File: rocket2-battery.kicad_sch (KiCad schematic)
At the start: 59 parts, among them J7 Conn_01x07, J8 SMA, J9 ARM Cortex Debug, P10 PAD_SMD, P5 PAD_SMD, P6 PAD_SMD, P7 PAD_SMD, P8 PAD_SMD, P9 PAD_SMD, Q2 Q_NMOS_GSD, Q3 Q_NMOS_GSD, Q4 PMOS, Q5 PMOS, Q6 Q_NMOS_GSD, Q7 Q_NMOS_GSD, Q8 PMOS, Q9 PMOS, U10 3V3 LDO, Y1 16MHz

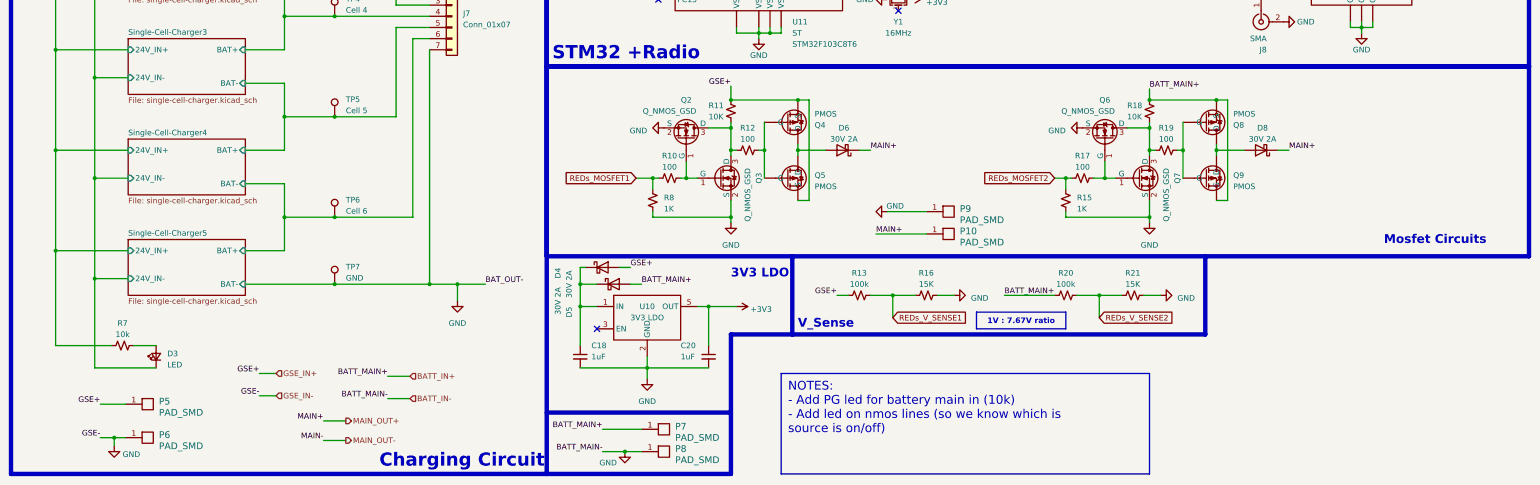
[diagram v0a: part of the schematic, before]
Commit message: Updated so only STM pins left really
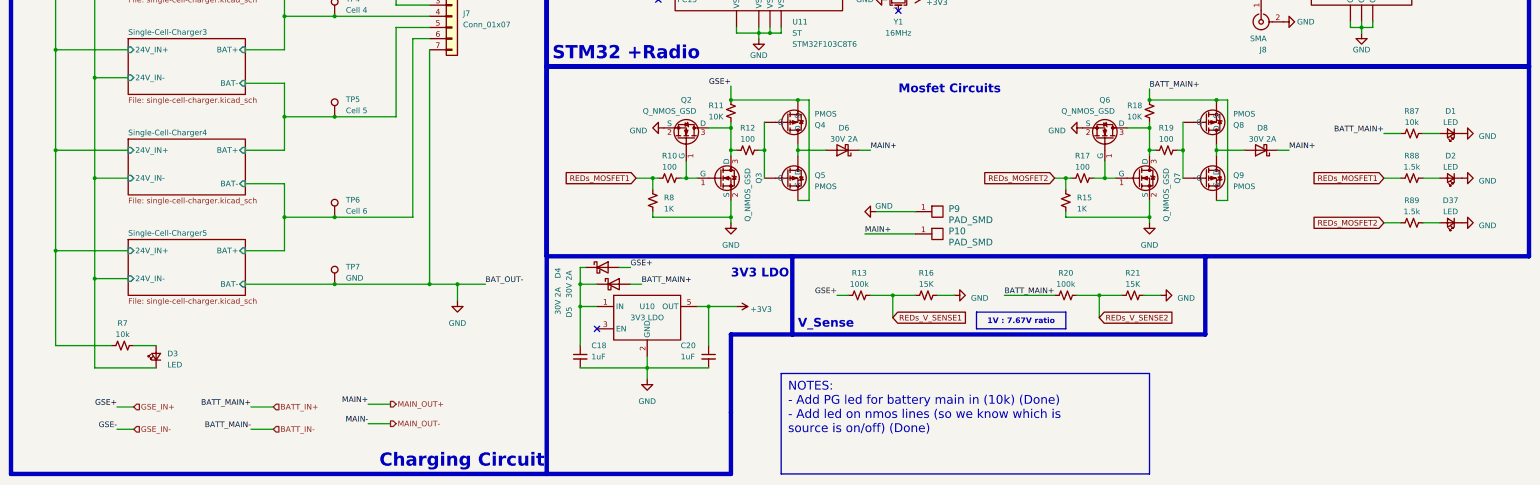
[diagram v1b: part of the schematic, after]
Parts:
- removed P5, P6, P7, P8: PAD_SMD, TestPoint:TestPoint_Pad_2.0x2.0mm, symbol pkl_misc:PAD_SMD
- added D1, D2, D37: LED, LED_SMD:LED_0603_1608Metric_Pad1.05x0.95mm_HandSolder, symbol Device:LED_Small
- added R87: 10k, Resistor_SMD:R_0603_1608Metric_Pad0.98x0.95mm_HandSolder, symbol Device:R_Small_US
- added R88, R89: 1.5k, Resistor_SMD:R_0603_1608Metric_Pad0.98x0.95mm_HandSolder, symbol Device:R_Small_US
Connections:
- net BATT_IN+: now also R87.1
- net GND: now also D1.1 (K), D2.1 (K), D37.1 (K); no longer D3.1 (K)
- net REDs_MOSFET1: now also R88.1
- net REDs_MOSFET2: now also R89.1
- new net: D2.2 (A), R88.2
- new net: D1.2 (A), R87.2
- new net: D37.2 (A), R89.2
- new net GSE_IN-: D3.1 (K)
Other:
- moved on the sheet: P10, P9

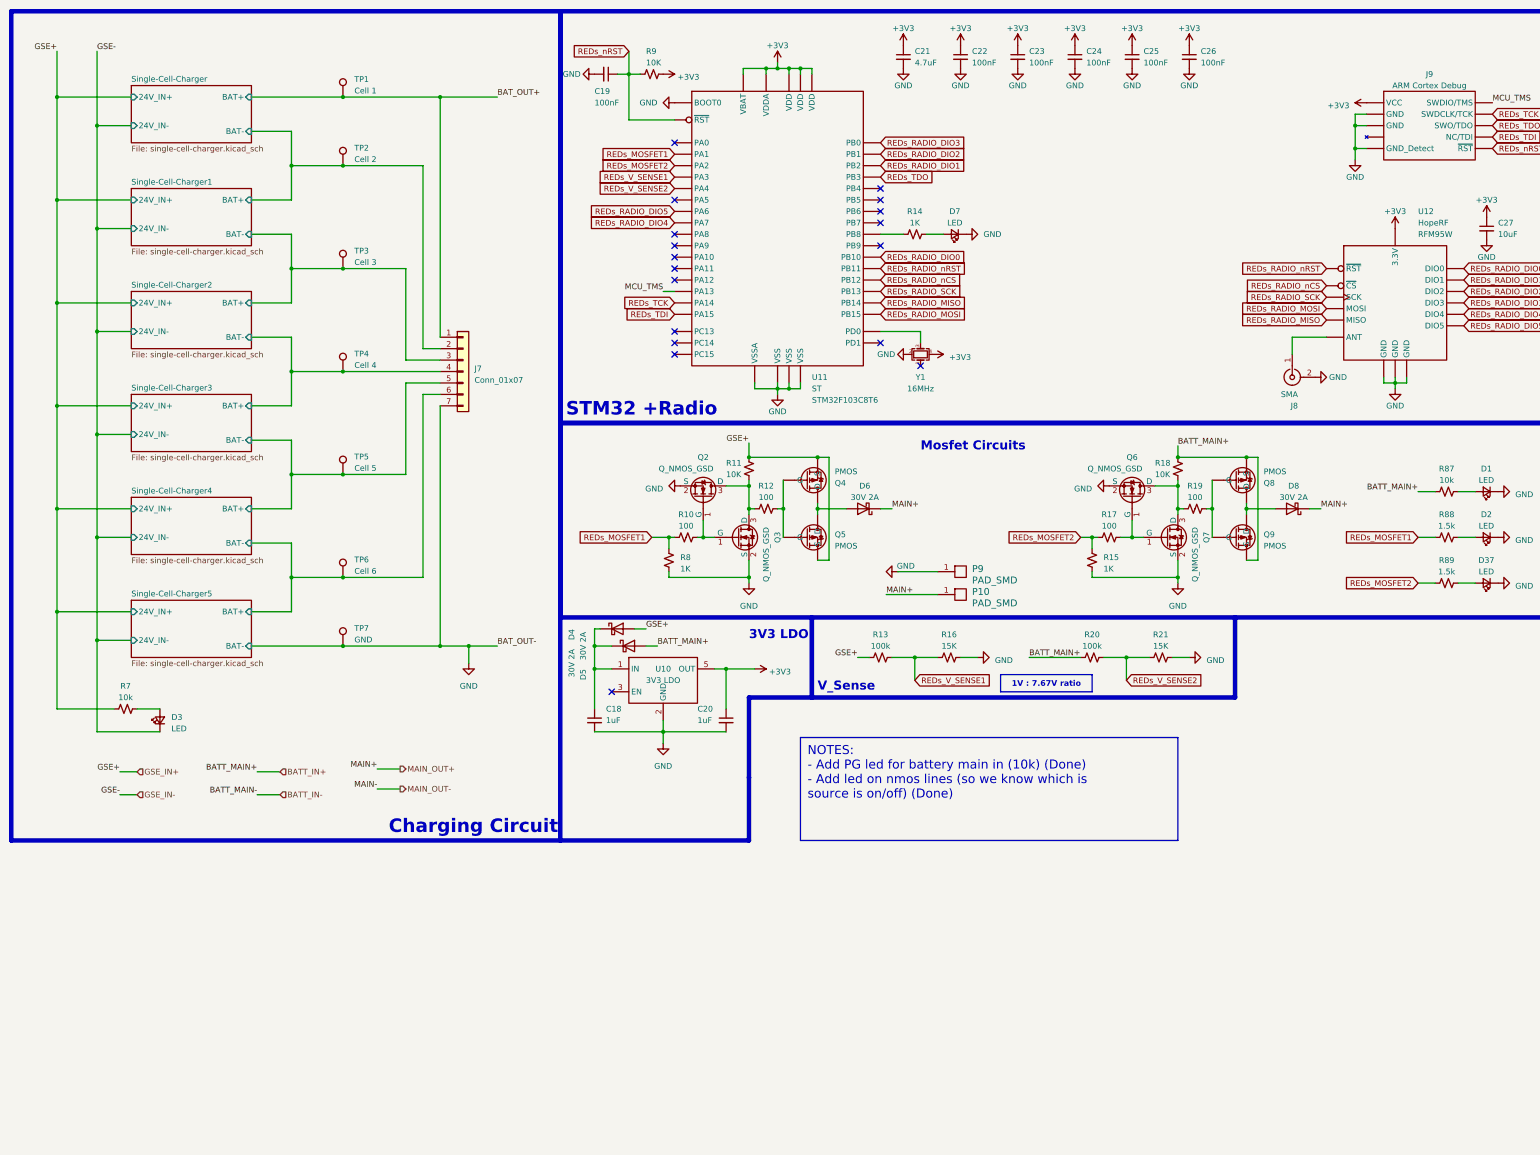
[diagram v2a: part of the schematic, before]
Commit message: Added stat sense in REDs; kicad V8.01
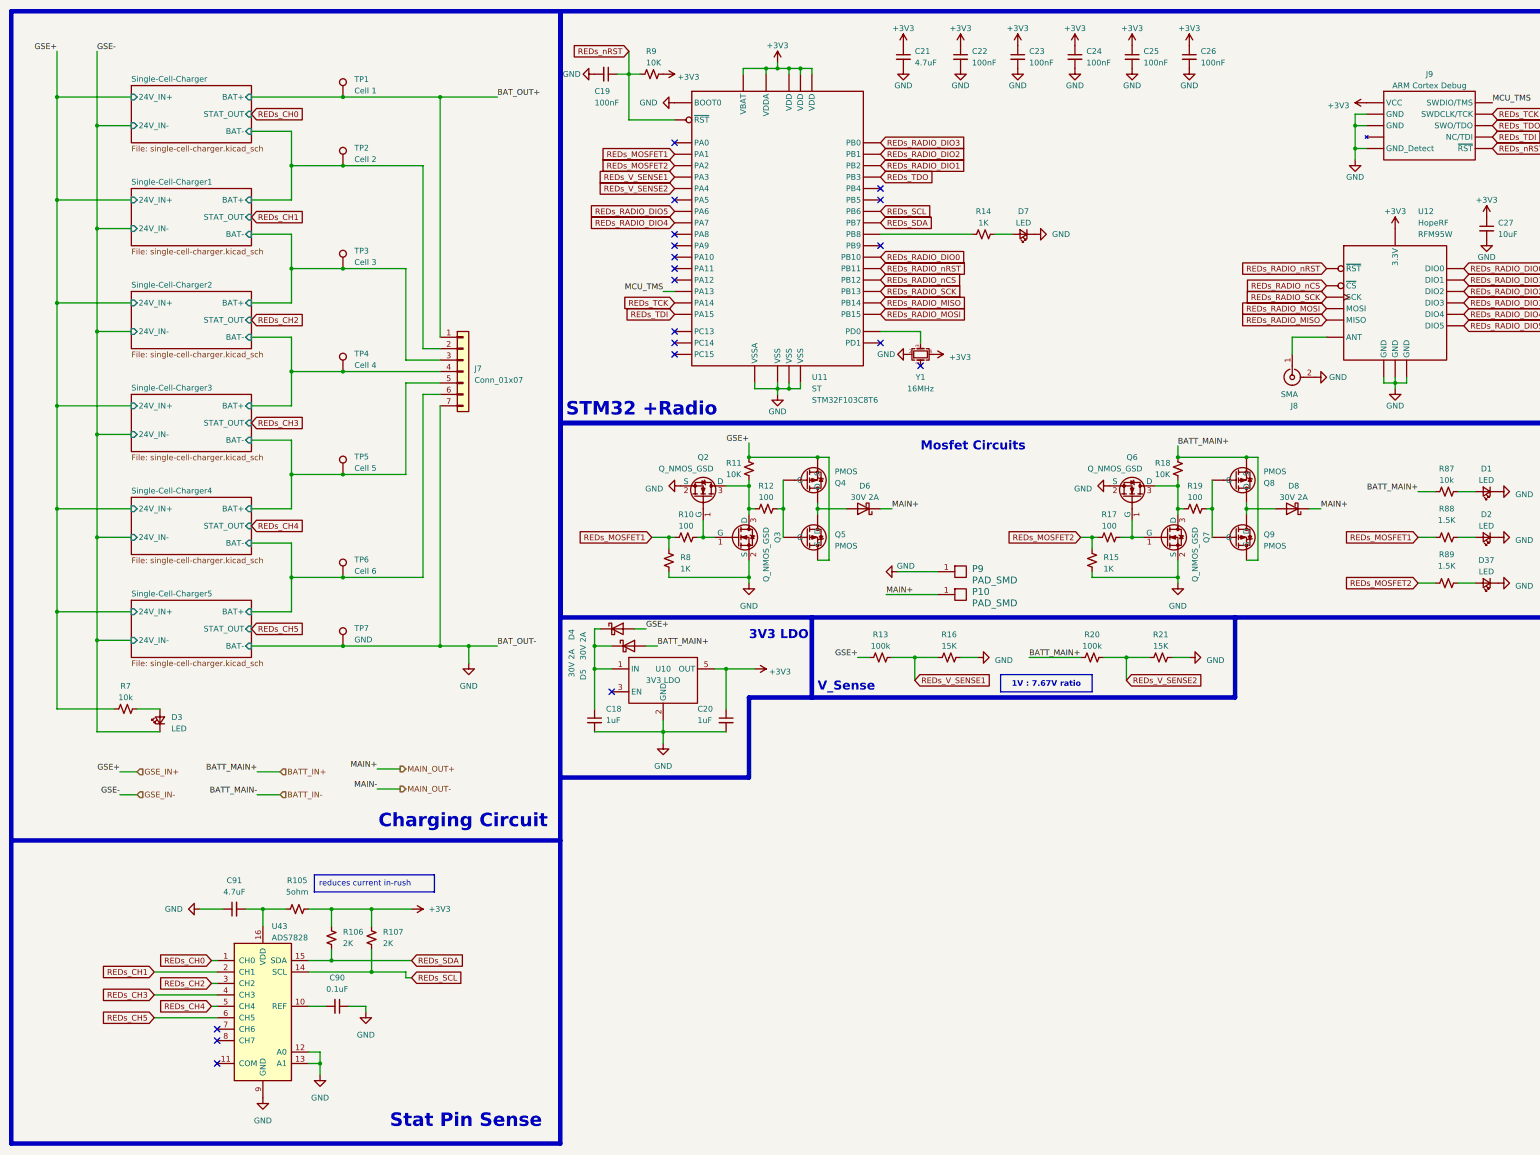
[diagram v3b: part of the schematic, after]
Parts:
- added C90: 0.1uF, symbol Device:C_Small
- added C91: 4.7uF, symbol Device:C_Small
- added R105: 5ohm, symbol Device:R_Small_US
- added R106, R107: 2K, symbol Device:R_Small_US
- added U43: ADS7828, Package_SO:TSSOP-16_4.4x5mm_P0.65mm, symbol Analog_ADC:ADS7828
- R88, R89: value 1.5k -> 1.5K
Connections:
- net +3V3: now also R105.2, R106.1, R107.1
- net GND: now also C90.1, C91.1, U43.12 (A0), U43.13 (A1), U43.9 (GND)
- net REDs_SCL: now reaches U11.42 (PB6)
- net REDs_SCL: now also R107.2, U43.14 (SCL)
- net REDs_SDA: now reaches U11.43 (PB7)
- net REDs_SDA: now also R106.2, U43.15 (SDA)
- new net: C90.2, U43.10 (REF)
- new net: C91.2, R105.1, U43.16 (VDD)
- new net REDs_CH0: U43.1 (CH0)
- new net REDs_CH1: U43.2 (CH1)
- new net REDs_CH2: U43.3 (CH2)
- new net REDs_CH3: U43.4 (CH3)
- new net REDs_CH4: U43.5 (CH4)
- new net REDs_CH5: U43.6 (CH5)
- no-connect marks 18 -> 19
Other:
- sheet Single-Cell-Charger ports: added STAT_OUT; removed none
- sheet Single-Cell-Charger1 ports: added STAT_OUT; removed none
- sheet Single-Cell-Charger2 ports: added STAT_OUT; removed none
- sheet Single-Cell-Charger3 ports: added STAT_OUT; removed none
- sheet Single-Cell-Charger4 ports: added STAT_OUT; removed none
- sheet Single-Cell-Charger5 ports: added STAT_OUT; removed none
- note added: "Stat Pin Sense"
- moved on the sheet: D7, R14

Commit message: 8.02 Update; Also changed VRMs and added some notes
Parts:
- renumbered C90 to C10, C18 to C11, C19 to C12, C20 to C13, C21 to C14, C22 to C15, C23 to C16, C24 to C17, C25 to C18, C26 to C19, C27 to C20, C91 to C9, D3 to D1, D4 to D2, D5 to D3, D6 to D4, D7 to D5, D8 to D6, D1 to D7, D2 to D8, D37 to D9, J7 to J3, J8 to J4, J9 to J5, P9 to P5, P10 to P6, R8 to R10, R10 to R11, R11 to R12, R12 to R13, R13 to R14, R16 to R15, R14 to R16, R15 to R17, R20 to R18, R17 to R19, R21 to R20, R18 to R21, R19 to R22, R87 to R23, R88 to R24, R89 to R25, R7 to R5, R105 to R6, R106 to R7, R107 to R8, U12 to U10, U43 to U7, U10 to U8, U11 to U9
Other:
- note added: "ONCE ROCKET IS LAUNCHED, IN NO CASE SHOULD IT KILL POWER. HOW TO ENSURE????"

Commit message: ECU essentially reviewable
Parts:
- removed C11, C13: 1uF, Capacitor_SMD:C_0603_1608Metric_Pad1.08x0.95mm_HandSolder, symbol Device:C_Small
- removed U8: 3V3 LDO, Package_SO:TSOP-5_1.65x3.05mm_P0.95mm, symbol UCIRP-KiCAD-Lib:NCV8730
- added C10, C11: 100uF, symbol Device:C_Polarized_Small
- added C12: 680uF, symbol Device:C_Polarized_Small
- added C13: 330uF, symbol Device:C_Polarized_Small
- added D10, D13, D9: LED, LED_SMD:LED_0603_1608Metric_Pad1.05x0.95mm_HandSolder, symbol Device:LED_Small
- added D4: 30V 2A, Diode_SMD:Nexperia_DSN1608-2_1.6x0.8mm, symbol Device:D_Schottky
- added D5: 30V 5A, Diode_SMD:D_SOD-128, symbol Device:D_Schottky
- added D6, D7: 700mV 5A, symbol Device:D_Schottky_Small
- added J3: USB_A, symbol Connector:USB_A
- added L1: 33uH, symbol Device:L_Small
- added L2: 68uH, symbol Device:L_Small
- added R17, R19: 1.5K, Resistor_SMD:R_0603_1608Metric_Pad0.98x0.95mm_HandSolder, symbol Device:R_Small_US
- added R25: 100k, Resistor_SMD:R_0603_1608Metric_Pad0.98x0.95mm_HandSolder, symbol Device:R_Small_US
- added R26: 10k, Resistor_SMD:R_0603_1608Metric_Pad0.98x0.95mm_HandSolder, symbol Device:R_Small_US
- added U6: LM2596S-3.3, Package_TO_SOT_SMD:TO-263-5_TabPin3, symbol Regulator_Switching:LM2596S-3.3
- added U7: LM2596S-5, Package_TO_SOT_SMD:TO-263-5_TabPin3, symbol Regulator_Switching:LM2596S-5
- D3: value 30V 2A -> 30V 5A; footprint Diode_SMD:Nexperia_DSN1608-2_1.6x0.8mm -> Diode_SMD:D_SOD-128; Manufacturer Onsemi -> Nexperia; Part # NSR20F30NXT5G -> PMEG3050EP,115
- U9: renamed from U10; Part # RFM95W -> RFM96W
- renumbered C9 to C7, C10 to C8, C12 to C9, D5 to D11, D6 to D12, D7 to D14, D8 to D15, D9 to D16, D4 to D8, J3 to J2, R9 to R10, R10 to R11, R11 to R12, R15 to R13, R12 to R14, R13 to R15, R18 to R16, R20 to R18, R16 to R20, R17 to R21, R19 to R22, R21 to R23, R22 to R24, R23 to R27, R24 to R28, R25 to R29, R14 to R9, U7 to U5, U9 to U8
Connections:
- net +3V3: now also C12.1, L1.2, R19.1, U6.4 (FB)
- net BATT_IN+: now also D4.2 (A), D5.2 (A); no longer D3.2 (A)
- net GND: now also C10.2, C11.2, C12.2, C13.2, D10.1 (K), D13.1 (K), D6.2 (A), D7.2 (A), D9.1 (K), J3.4 (GND), J3.5 (Shield), U6.3 (GND), U6.5 (~{ON}/OFF), U7.3 (GND), U7.5 (~{ON}/OFF)
- net GSE_IN+: now also D3.2 (A), R26.1
- net REDs_RADIO_DIO2: no longer U9.16 (DIO2)
- net REDs_RADIO_nCS: now also R25.2
- net at D3.1 (K): now also C11.1, D5.1 (K), U7.1 (VIN); no longer D2.1 (K)
- net REDs_RADIO_DIO3: no longer names the net of U9.11 (DIO3)
- net REDs_RADIO_DIO3: no longer U8.18 (PB0)
- net REDs_RADIO_DIO4: no longer names the net of U9.12 (DIO4)
- net REDs_RADIO_DIO4: no longer U8.17 (PA7)
- net REDs_RADIO_DIO5: no longer names the net of U9.7 (DIO5)
- net REDs_RADIO_DIO5: no longer U8.16 (PA6)
- new net: C13.1, J3.1 (VBUS), L2.2, R17.1, U7.4 (FB)
- new net: D9.2 (A), R17.2
- new net: D7.1 (K), L2.1, U7.2 (OUT)
- new net: D10.2 (A), R19.2
- new net: D6.1 (K), L1.1, U6.2 (OUT)
- new net: C10.1, D2.1 (K), D4.1 (K), U6.1 (VIN)
- new net: D13.2 (A), R26.2
- new net +3.3V: R25.1
- no-connect marks 19 -> 27
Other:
- note added: "3V3 REG"
- note added: "5V 3A Insta360"
- note added: "Power only from GS?"
- note removed: "3V3 LDO"
- note removed: "ONCE ROCKET IS LAUNCHED, IN NO CASE SHOULD IT KILL POWER. HOW TO ENSURE????"
- moved on the sheet: R13, R16, R18, R9

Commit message: addressed PR comments
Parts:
- removed D5: 30V 5A, Diode_SMD:D_SOD-128, symbol Device:D_Schottky
- removed J3: USB_A, symbol Connector:USB_A
- added J3: ~, Connector_USB:USB_C_Receptacle_GCT_USB4105-xx-A_16P_TopMnt_Horizontal, symbol 0INSP-KICAD-LIB:USB-C
- renumbered D11 to D10, D12 to D11, D13 to D12, D14 to D13, D15 to D14, D16 to D15, D6 to D5, D7 to D6, D8 to D7, D9 to D8, D10 to D9
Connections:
- net GND: now also J3.A1 (GND), J3.A12 (GND), J3.B1 (GND), J3.B12 (GND)
- net at C13.1, L2.2, R17.1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: now also J3.A4 (VBUS), J3.A9 (VBUS), J3.B4 (VBUS), J3.B9 (VBUS)
- no-connect marks 27 -> 41
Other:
- note added: "Power only from GS"
- note removed: "Power only from GS?"
- moved on the sheet: D3

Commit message: Updated schematic with IOC
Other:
- note added: "Power reg circuits taken from WEBENCH. Component reliability should be good."
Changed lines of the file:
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@@
+		)
+	)
+	(text "Power reg circuits taken from WEBENCH.\nComponent reliability should be good."
+		(exclude_from_sim no)
+		(at 253.492 189.23 0)
+		(effects
+			(font
+				(size 1.27 1.27)
+				(color 255 56 91 1)
+			)
 		)
 	)
